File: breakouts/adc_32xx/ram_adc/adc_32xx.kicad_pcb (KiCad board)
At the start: 4 copper layers, 97 parts, among them J201 Conn_Coaxial, J202 Conn_Coaxial, J203 Conn_02x06_Odd_Even, J204 Conn_02x20_Odd_Even, J205 Conn_01x07, J301 Conn_Coaxial, J401 Conn_Coaxial, J501 Conn_01x01, J502 Conn_01x01, T301 MABAES0060, T302 MABAES0060, T401 MABAES0060, T402 MABAES0060, U201 VEMI65AB-HCI, U202 ADC322x, U501 ADM7170

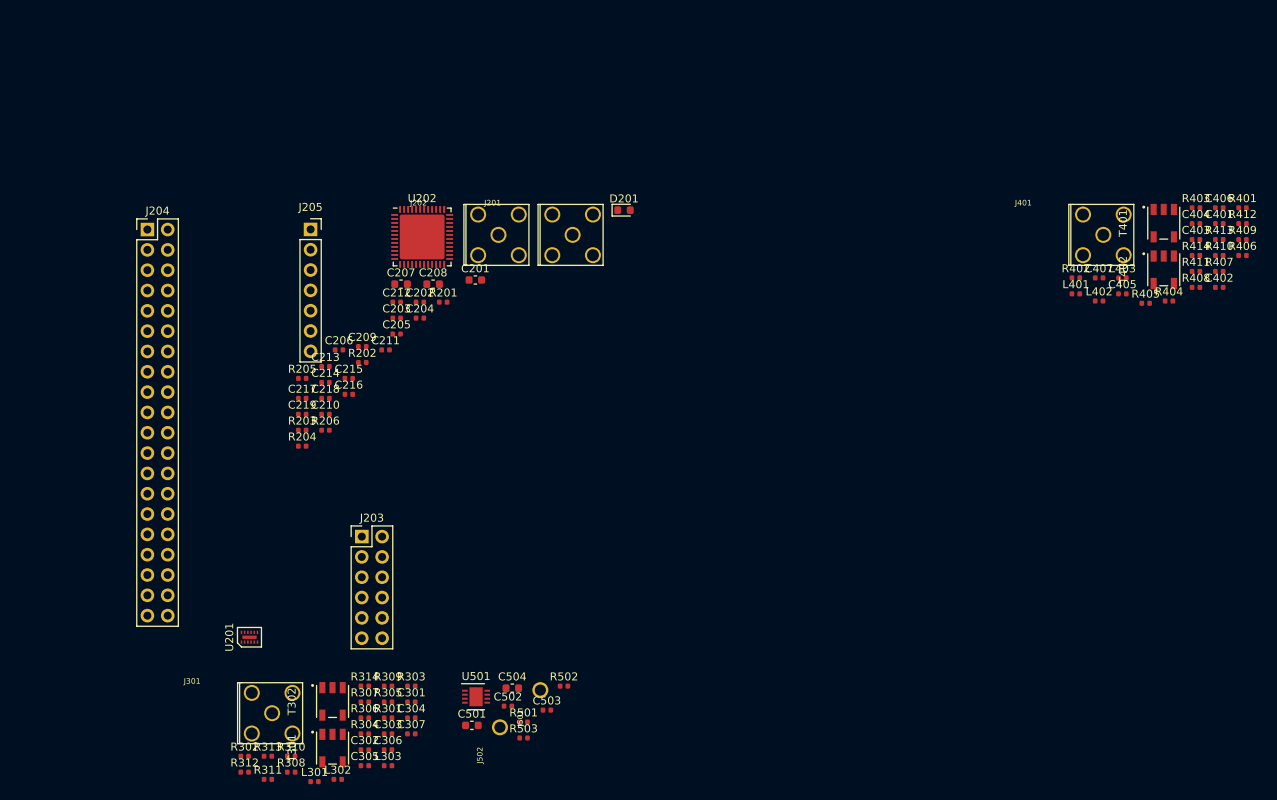
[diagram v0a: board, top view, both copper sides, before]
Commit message: component placement for adc322x breakout
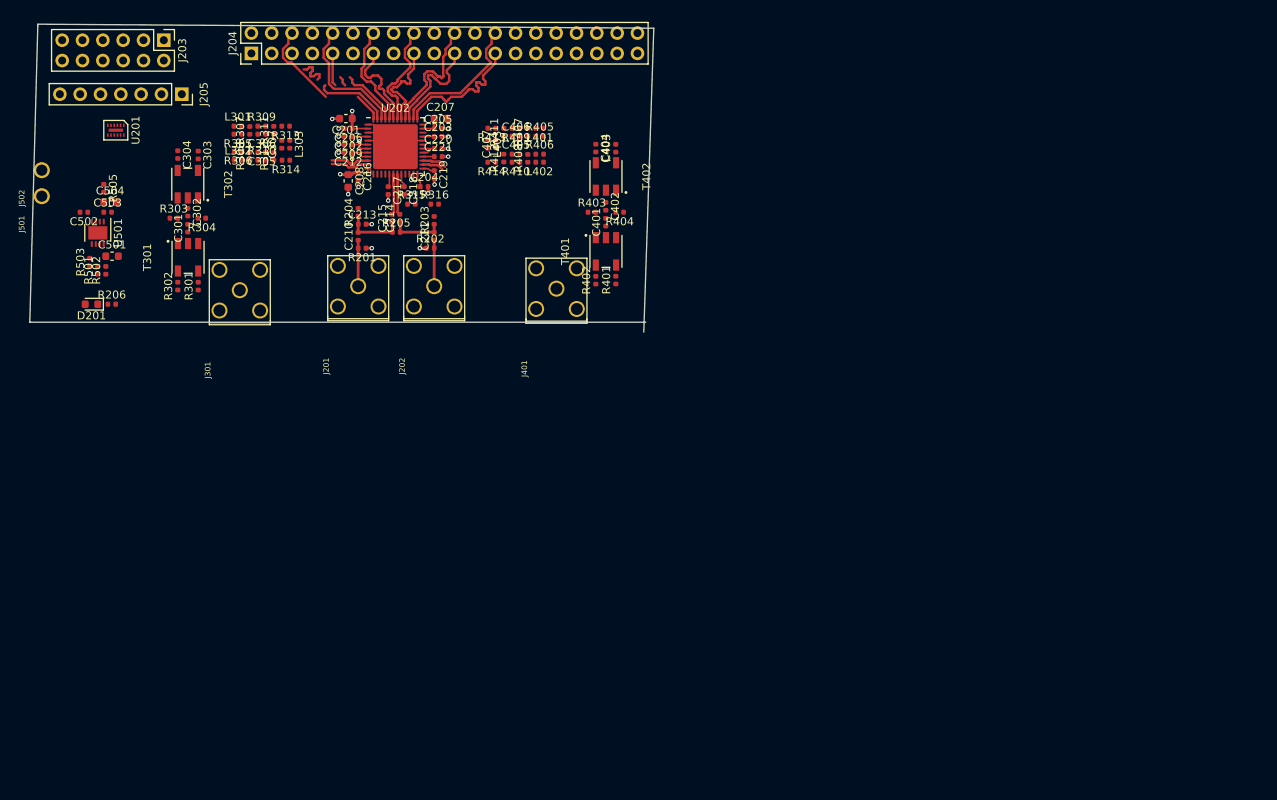
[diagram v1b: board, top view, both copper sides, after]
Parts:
- added C220: 100 nF, Capacitor_SMD:C_0402_1005Metric, F.Cu at (91.5, 55.3)
- added C221: 100 nF, Capacitor_SMD:C_0402_1005Metric, F.Cu at (91.5, 56.3)
- added R315: DNI, Resistor_SMD:R_0402_1005Metric, F.Cu at (88.2, 62.2)
- added R316: DNI, Resistor_SMD:R_0402_1005Metric, F.Cu at (91.1, 62.2)
- added R505: DNI, Resistor_SMD:R_0402_1005Metric, F.Cu at (49.8, 60.2)
- moved R412 92.7 mm to (99.8, 56.5), turned to 90 degrees
- moved R413 92.0 mm to (98.2, 52.8), turned to 180 degrees
- moved R409 91.9 mm to (101.3, 52.8), turned to 180 degrees
- moved J502 90.2 mm to (42.0, 58.0)
- moved R414 88.8 mm to (98.2, 57.0), turned to 180 degrees
- moved R406 88.8 mm to (104.2, 56.0)
- moved R410 88.7 mm to (101.3, 57.0), turned to 180 degrees
- moved C406 88.4 mm to (101.3, 53.8)
- moved R411 88.3 mm to (99.8, 53.2), turned to 90 degrees
- moved R407 88.2 mm to (102.8, 53.2), turned to 90 degrees
- moved J501 87.7 mm to (42.0, 61.2)
- moved R408 85.1 mm to (102.8, 56.5), turned to 90 degrees
- moved C503 83.0 mm to (50.2, 63.2)
- moved L301 82.5 mm to (66.5, 52.5)
- moved C502 81.4 mm to (47.3, 63.2), turned to 180 degrees
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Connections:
- net /adc/IN_A_M renamed /adc/IN_A_N
- net /adc/IN_B_M renamed /adc/IN_B_N
- C503 pad 1: +1V8 -> Net-(C503-Pad1)
- C504 pad 1: +1V8 -> Net-(C503-Pad1)
- J201 pad 1: GND -> Net-(C210-Pad1)
- J201 pad 2: Net-(C210-Pad1) -> GND
- J202 pad 1: GND -> Net-(C211-Pad1)
- J202 pad 2: Net-(C211-Pad1) -> GND
- J204 pad 10: /adc/DB0_N -> /adc/DA1_N
- J204 pad 13: /adc/FCLK_P -> /adc/DCLK_P
- J204 pad 14: /adc/FCLK_N -> /adc/DCLK_N
- J204 pad 17: /adc/DCLK_P -> /adc/FCLK_P
- J204 pad 18: /adc/DCLK_N -> /adc/FCLK_N
- J204 pad 21: /adc/DA1_P -> /adc/DB0_P
- J204 pad 22: /adc/DA1_N -> /adc/DB0_N
- J204 pad 25: /adc/DA0_P -> /adc/DB1_P
- J204 pad 26: /adc/DA0_N -> /adc/DB1_N
- J204 pad 29: (no net) -> /adc/CLK_FPGA_P
- J204 pad 30: (no net) -> /adc/CLK_FPGA_N
- J204 pad 5: /adc/DB1_P -> /adc/DA0_P
- J204 pad 6: /adc/DB1_N -> /adc/DA0_N
- J204 pad 9: /adc/DB0_P -> /adc/DA1_P
- J301 pad 1: GND -> Net-(J301-Pad1)
- J301 pad 2: Net-(J301-Pad2) -> GND
- J401 pad 1: GND -> Net-(J401-Pad1)
- J401 pad 2: Net-(J401-Pad2) -> GND
- R204 pad 2: /adc/CLK_FPGA_P -> /adc/CLK_FPGA_N
- R301 pad 1: Net-(J301-Pad2) -> Net-(J301-Pad1)
- R401 pad 1: Net-(J401-Pad2) -> Net-(J401-Pad1)
- U501 pad 1: +1V8 -> Net-(C503-Pad1)
- U501 pad 2: +1V8 -> Net-(C503-Pad1)
- U501 pad 3: +1V8 -> Net-(R315-Pad2)
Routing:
- net +1V8: track 0.00 -> 31.5 mm, vias 0 -> 4
- net GND: track 0.00 -> 30.4 mm, vias 0 -> 18
- net /adc/DB1_N: track 0.00 -> 17.7 mm
- net /adc/DB1_P: track 0.00 -> 17.7 mm
- net /adc/DA1_N: track 0.00 -> 16.2 mm
- net /adc/DB0_N: track 0.00 -> 15.9 mm
- net /adc/DA0_N: track 0.00 -> 14.5 mm
- net /adc/DA0_P: track 0.00 -> 14.5 mm
- net /adc/DB0_P: track 0.00 -> 13.9 mm
- net /adc/FCLK_N: track 0.00 -> 13.7 mm
- net /adc/DCLK_N: track 0.00 -> 13.2 mm
- net /adc/DA1_P: track 0.00 -> 13.0 mm
- net /adc/FCLK_P: track 0.00 -> 12.2 mm
- net /adc/DCLK_P: track 0.00 -> 11.8 mm
- net Net-(C210-Pad2): track 0.00 -> 7.73 mm
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- added copper zone on In1.Cu, net GND
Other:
- board outline added: 78 x 38.5 mm
- net class LVDS added: clearance 0.127, trace_width 0.3048, via_dia 0.56, via_drill 0.3

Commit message: finished layout of adc32xx ecp5 board
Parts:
- added G***: LOGO, vna_footprints:cat, B.Cu at (97.8, 57.5)
- moved R316 42.1 mm to (49.0, 61.5), turned to 180 degrees
- moved R315 38.5 mm to (49.8, 60.5), turned to 180 degrees
- moved R501 33.5 mm to (65.2, 41.2), turned to 180 degrees
- moved R502 25.7 mm to (46.8, 45.0), turned to 0 degrees
- moved D201 17.7 mm to (52.2, 57.5)
- moved R206 17.7 mm to (54.8, 57.5)
- moved J502 7.42 mm to (48.2, 54.0)
- moved J501 7.16 mm to (48.2, 57.8)
- moved J205 2.80 mm to (62.0, 47.2)
- moved U201 2.80 mm to (53.8, 51.8)
- moved J203 2.29 mm to (58.9, 40.1)
- moved C501 1.82 mm to (52.5, 68.2)
- moved C502 1.82 mm to (49.0, 62.8)
- moved C503 1.82 mm to (52.0, 62.8)
- moved C504 1.82 mm to (52.3, 61.5)
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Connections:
- U501 pad 6: (no net) -> GND
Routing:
- net +1V8: track 31.5 -> 128.8 mm, vias 4 -> 10
- net Net-(C501-Pad1): track 0.00 -> 53.7 mm
- net /VCM: track 1.71 -> 54.9 mm, vias 0 -> 7
- net Net-(U201-Pad7): track 0.00 -> 48.2 mm, vias 0 -> 4
- net Net-(U201-Pad8): track 0.00 -> 47.5 mm, vias 0 -> 2
- net Net-(U201-Pad9): track 0.00 -> 42.4 mm, vias 0 -> 2
- net Net-(U201-Pad10): track 0.00 -> 40.3 mm, vias 0 -> 2
- net /adc/CLK_FPGA_N: track 0.00 -> 38.6 mm, vias 0 -> 1
- net /adc/CLK_FPGA_P: track 0.00 -> 38.5 mm, vias 0 -> 1
- net Net-(U201-Pad11): track 0.00 -> 38.0 mm, vias 0 -> 2
- net Net-(U201-Pad12): track 0.00 -> 36.1 mm, vias 0 -> 2
- net /adc/SYSREF_N: track 0.04 -> 33.7 mm, vias 0 -> 2
- net /adc/SYSREF_P: track 0.04 -> 32.8 mm, vias 0 -> 2
- net /adc/EN: track 0.00 -> 31.9 mm, vias 0 -> 2
- net /adc/RESET: track 0.00 -> 29.7 mm
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- added copper zone on B.Cu, net GND
- added copper zone on F.Cu, net GND
- added copper zone on In2.Cu, net GND
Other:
- board size 78 x 38.5 mm -> 72.8 x 38.2 mm
- rule solder_mask_min_width: 0.25 -> 0.15
- board text added: "0V"
- board text added: "ADC33XX ECP5 VERSA BREADBOARD 2020.5"
- board text added: "CLK"
- board text added: "CLK N"
- board text added: "CLK P"
- board text added: "DAT"
- board text added: "GND"
- board text added: "IN A"
- board text added: "IN B"
- board text added: "PDN"
- board text added: "RST"
- board text added: "SDO"
- board text added: "SEN"
